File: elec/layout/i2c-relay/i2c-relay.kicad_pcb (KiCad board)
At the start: 2 copper layers, 7 parts, among them U2 10kΩ ±1% 62.5mW, U3 1kΩ ±1% 62.5mW

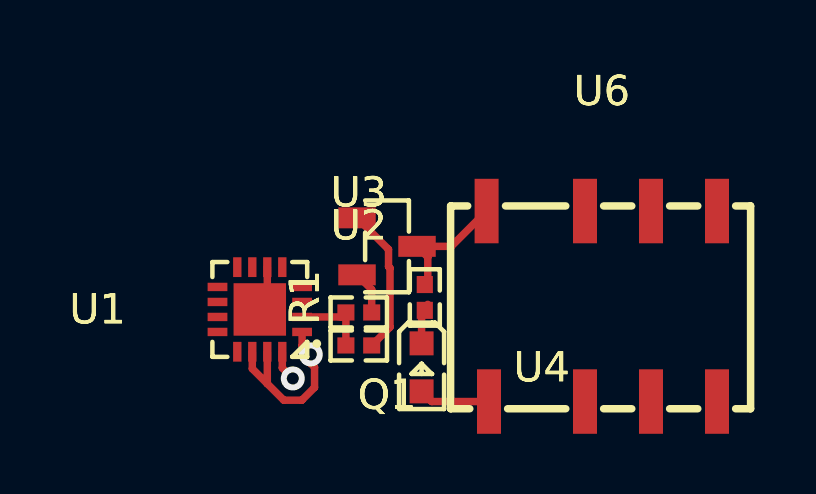
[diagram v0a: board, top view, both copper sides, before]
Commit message: update i2c relay
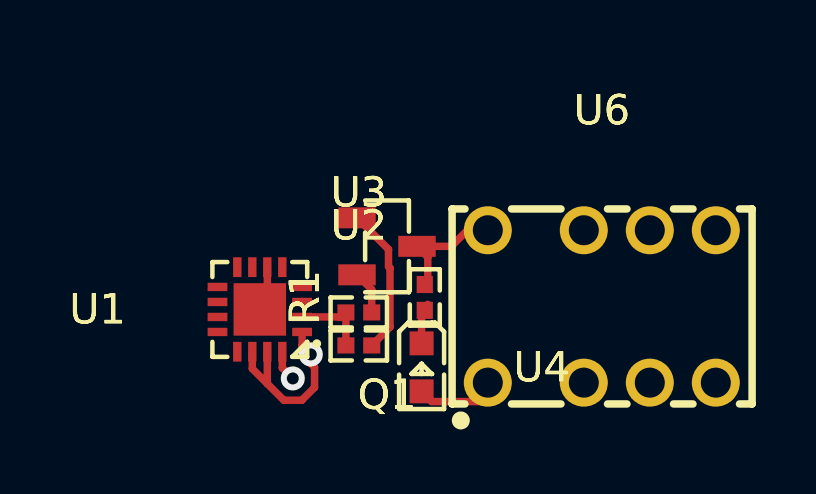
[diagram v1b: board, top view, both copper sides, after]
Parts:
- U6: footprint lib:RELAY-SMD_HFD4-5-SR -> atopile:RELAY-TH_HFDXXX-689a1e
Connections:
- net VCCP renamed RESET
- Q1 pad 2: gnd-1 -> gnd-3
- U1 pad 10: gpio_expander-net-3 -> gpio_expander-net-4
- U1 pad 12: line -> line-2
- U1 pad 13: line-2 -> line
- U1 pad 17: gnd -> gnd-1
- U1 pad 3: gpio_expander-net-5 -> gpio_expander-net
- U1 pad 4: gpio_expander-net-2 -> gpio_expander-net-1
- U1 pad 5: gpio_expander-net-1 -> gpio_expander-net-6
- U1 pad 6: gnd -> gnd-1
- U1 pad 7: gpio_expander-net -> gpio_expander-net-5
- U1 pad 8: gpio_expander-net-6 -> gpio_expander-net-3
- U1 pad 9: gpio_expander-net-4 -> gpio_expander-net-2
- U3 pad 2: gnd-1 -> gnd-3
- U6 pad 2: (no net) -> relay.relay.footprint.pins[1].net-net
- U6 pad 3: gnd-3 -> gnd-2
- U6 pad 4: gnd-2 -> gnd
- U6 pad 7: (no net) -> relay.relay.footprint.pins[6].net-net
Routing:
- net gnd: track 2.55 -> 0.00 mm, vias 1 -> 0
- net gnd-3: track 0.00 -> 1.46 mm
- net ADDR: track 0.00 -> 1.03 mm, vias 0 -> 1

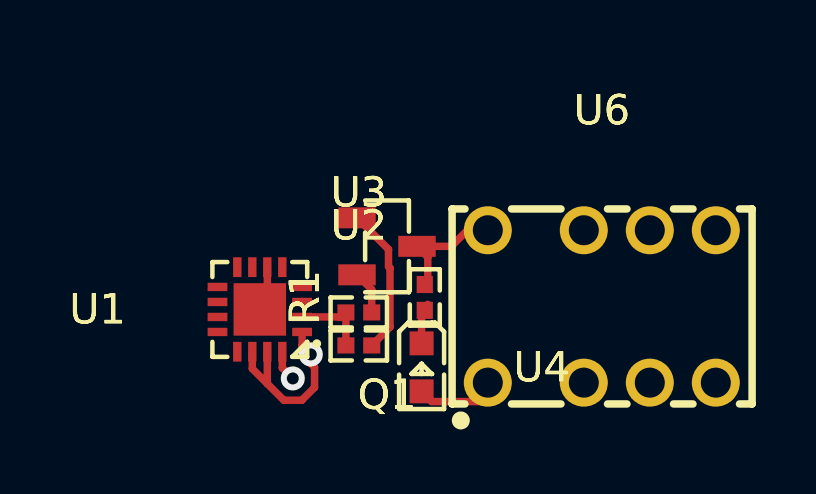
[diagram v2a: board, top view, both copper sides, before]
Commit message: fix i2c-relay layout
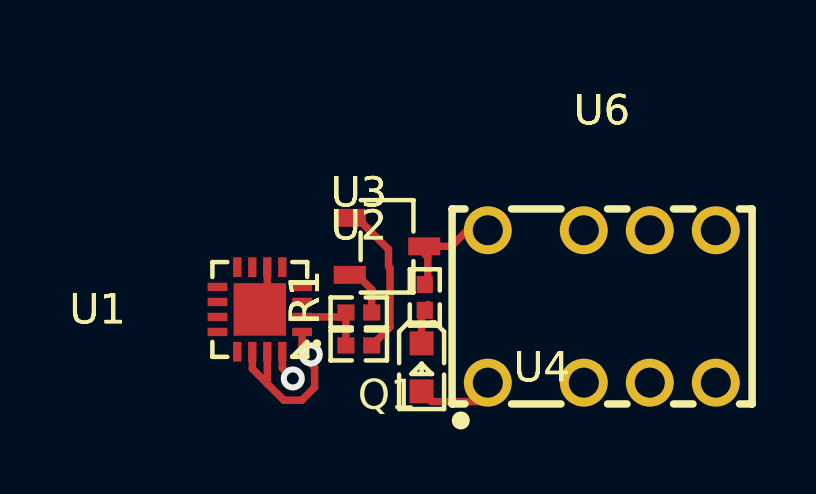
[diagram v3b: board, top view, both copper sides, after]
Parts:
- Q1: footprint atopile:SOT-23-3_L2.9-W1.3-P1.90-LS2.4-BR-688f29 -> atopile:SOT-23-3_L2.9-W1.6-P1.90-LS2.8-BR-186170
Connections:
- net RESET renamed VCCI
- net line-2 renamed SCL
- U1 pad 13: line -> SDA
- U1 pad 2: line-1 -> line
- U1 pad 3: gpio_expander-net -> gpio_expander-net-3
- U1 pad 4: gpio_expander-net-1 -> gpio_expander-net
- U1 pad 7: gpio_expander-net-5 -> gpio_expander-net-2
- U1 pad 8: gpio_expander-net-3 -> gpio_expander-net-1
- U1 pad 9: gpio_expander-net-2 -> gpio_expander-net-5
- U2 pad 1: line-1 -> line
- U3 pad 1: line-1 -> line
- U4 pad 2: hv-2 -> hv-1
- U6 pad 1: hv-2 -> hv-1
- U6 pad 5: hv -> hv-2
- U6 pad 6: hv-1 -> hv
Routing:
- net line-1: track 2.62 -> 0.00 mm
- net line: track 0.00 -> 2.62 mm
- net hv-2: track 2.39 -> 0.00 mm
- net hv-1: track 0.00 -> 2.39 mm

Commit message: building frozen
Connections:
- net VCCI renamed RESET
- Q1 pad 2: gnd-3 -> gnd
- U1 pad 10: gpio_expander-net-4 -> gpio_expander-net-5
- U1 pad 17: gnd-1 -> gnd-2
- U1 pad 3: gpio_expander-net-3 -> gpio_expander-net-1
- U1 pad 4: gpio_expander-net -> gpio_expander-net-6
- U1 pad 5: gpio_expander-net-6 -> gpio_expander-net
- U1 pad 6: gnd-1 -> gnd-2
- U1 pad 7: gpio_expander-net-2 -> gpio_expander-net-3
- U1 pad 8: gpio_expander-net-1 -> gpio_expander-net-4
- U1 pad 9: gpio_expander-net-5 -> gpio_expander-net-2
- U3 pad 2: gnd-3 -> gnd
- U4 pad 2: hv-1 -> hv
- U6 pad 1: hv-1 -> hv
- U6 pad 3: gnd-2 -> gnd-1
- U6 pad 4: gnd -> gnd-3
- U6 pad 5: hv-2 -> hv-1
- U6 pad 6: hv -> hv-2
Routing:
- net hv-1: track 2.39 -> 0.00 mm
- net hv: track 0.00 -> 2.39 mm
- net gnd-2: track 0.00 -> 1.51 mm
- net gnd-1: track 1.51 -> 0.00 mm
- net gnd-3: track 1.46 -> 0.00 mm
- net gnd: track 0.00 -> 1.46 mm
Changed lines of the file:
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@@
         (legacy_teardrops no)
     )
-    (paper A4)
+    (paper "A4")
     (layers
         (0 "F.Cu" signal)
@@
         (tenting front back)
         (pcbplotparams
-            (layerselection "0x00000000_00000000_55555555_5755f5ff")
-            (plot_on_all_layers_selection "0x00000000_00000000_00000000_00000000")
+            (layerselection 0x00000000_00000000_55555555_5755f5ff)
+            (plot_on_all_layers_selection 0x00000000_00000000_00000000_00000000)
             (disableapertmacros no)
             (usegerberextensions no)
@@
             (dxfusepcbnewfont yes)
             (psnegative no)
+            (psa4output no)
             (plot_black_and_white yes)
-            (psa4output no)
+            (plotinvisibletext no)
+            (sketchpadsonfab no)
             (plotreference yes)
+            (plotvalue yes)
             (plotpadnumbers no)
             (hidednponfab no)
             (sketchdnponfab yes)
             (crossoutdnponfab yes)
-            (plotvalue yes)
             (plotfptext yes)
-            (plotinvisibletext no)
-            (sketchpadsonfab no)
             (subtractmaskfromsilk no)
             (outputformat 1)
@@
     )
     (net 0 "")
-    (net 1 "gpio_expander-net")
+    (net 1 "gpio_expander-net-6")
     (net 2 "SCL")
-    (net 3 "gpio_expander-net-4")
-    (net 4 "hv")
-    (net 5 "gpio_expander-net-2")
-    (net 6 "gpio_expander-net-5")
-    (net 7 "hv-1")
+    (net 3 "gpio_expander-net-5")
+    (net 4 "hv-2")
+    (net 5 "gpio_expander-net-3")
+    (net 6 "gpio_expander-net-2")
+    (net 7 "hv")
     (net 8 "line")
-    (net 9 "gnd-2")
+    (net 9 "gnd-1")
     (net 10 "INT")
-    (net 11 "gpio_expander-net-1")
-    (net 12 "VCCI")
-    (net 13 "hv-2")
+    (net 11 "gpio_expander-net-4")
+    (net 12 "RESET")
+    (net 13 "hv-1")
     (net 14 "SDA")
-    (net 15 "gpio_expander-net-6")
-    (net 16 "gnd")
-    (net 17 "gnd-3")
+    (net 15 "gpio_expander-net")
+    (net 16 "gnd-3")
+    (net 17 "gnd")
     (net 18 "gate")
-    (net 19 "gpio_expander-net-3")
-    (net 20 "gnd-1")
+    (net 19 "gpio_expander-net-1")
+    (net 20 "gnd-2")
     (net 21 "relay-gnd")
     (net 22 "cathode")
@@
             (size 0.57 0.54)
             (layers "F.Cu" "F.Mask" "F.Paste")
-            (net 17 "gnd-3")
+            (net 17 "gnd")
             (remove_unused_layers yes)
             (keep_end_layers yes)
@@
             (size 0.8 0.8)
             (layers "F.Cu" "F.Mask" "F.Paste")
-            (net 7 "hv-1")
+            (net 7 "hv")
             (remove_unused_layers yes)
             (keep_end_layers yes)
@@
             (drill 0.999998)
             (layers "*.Cu" "*.Mask")
-            (net 7 "hv-1")
+            (net 7 "hv")
             (remove_unused_layers no)
             (keep_end_layers yes)
@@
             (drill 0.999998)
             (layers "*.Cu" "*.Mask")
-            (net 9 "gnd-2")
+            (net 9 "gnd-1")
             (remove_unused_layers no)
             (keep_end_layers yes)
@@
             (drill 0.999998)
             (layers "*.Cu" "*.Mask")
-            (net 16 "gnd")
+            (net 16 "gnd-3")
             (remove_unused_layers no)
             (keep_end_layers yes)
@@
             (drill 0.999998)
             (layers "*.Cu" "*.Mask")
-            (net 13 "hv-2")
+            (net 13 "hv-1")
             (remove_unused_layers no)
             (keep_end_layers yes)
@@
             (drill 0.999998)
             (layers "*.Cu" "*.Mask")
-            (net 4 "hv")
+            (net 4 "hv-2")
             (remove_unused_layers no)
             (keep_end_layers yes)
@@
             (size 1.07 0.6)
             (layers "F.Cu" "F.Paste" "F.Mask")
-            (net 17 "gnd-3")
+            (net 17 "gnd")
             (remove_unused_layers yes)
             (keep_end_layers yes)
@@
             (size 0.28 0.66)
             (layers "F.Cu" "F.Mask" "F.Paste")
-            (net 12 "VCCI")
+            (net 12 "RESET")
             (remove_unused_layers yes)
             (keep_end_layers yes)
@@
             (size 0.28 0.66)
             (layers "F.Cu" "F.Mask" "F.Paste")
-            (net 19 "gpio_expander-net-3")
+            (net 19 "gpio_expander-net-1")
             (remove_unused_layers yes)
             (keep_end_layers yes)
@@
             (size 0.28 0.66)
             (layers "F.Cu" "F.Mask" "F.Paste")
-            (net 1 "gpio_expander-net")
+            (net 1 "gpio_expander-net-6")
             (remove_unused_layers yes)
             (keep_end_layers yes)
@@
             (size 0.66 0.28)
             (layers "F.Cu" "F.Mask" "F.Paste")
-            (net 15 "gpio_expander-net-6")
+            (net 15 "gpio_expander-net")
             (remove_unused_layers yes)
             (keep_end_layers yes)
@@
             (size 0.66 0.28)
             (layers "F.Cu" "F.Mask" "F.Paste")
-            (net 20 "gnd-1")
+            (net 20 "gnd-2")
             (remove_unused_layers yes)
             (keep_end_layers yes)
@@
             (size 0.66 0.28)
             (layers "F.Cu" "F.Mask" "F.Paste")
-            (net 5 "gpio_expander-net-2")
+            (net 5 "gpio_expander-net-3")
             (remove_unused_layers yes)
             (keep_end_layers yes)
@@
             (size 0.66 0.28)
             (layers "F.Cu" "F.Mask" "F.Paste")
-            (net 11 "gpio_expander-net-1")
+            (net 11 "gpio_expander-net-4")
             (remove_unused_layers yes)
             (keep_end_layers yes)
@@
             (size 0.28 0.66)
             (layers "F.Cu" "F.Mask" "F.Paste")
-            (net 6 "gpio_expander-net-5")
+            (net 6 "gpio_expander-net-2")
             (remove_unused_layers yes)
             (keep_end_layers yes)
@@
             (size 0.28 0.66)
             (layers "F.Cu" "F.Mask" "F.Paste")
-            (net 3 "gpio_expander-net-4")
+            (net 3 "gpio_expander-net-5")
             (remove_unused_layers yes)
             (keep_end_layers yes)
@@
             (size 0.66 0.28)
             (layers "F.Cu" "F.Mask" "F.Paste")
-            (net 12 "VCCI")
+            (net 12 "RESET")
             (remove_unused_layers yes)
             (keep_end_layers yes)
@@
             (size 0.66 0.28)
             (layers "F.Cu" "F.Mask" "F.Paste")
-            (net 12 "VCCI")
+            (net 12 "RESET")
             (remove_unused_layers yes)
             (keep_end_layers yes)
@@
             (size 1.75 1.75)
             (layers "F.Cu" "F.Mask" "F.Paste")
-            (net 20 "gnd-1")
-            (remove_unused_layers yes)
-            (keep_end_layers yes)
+            (net 20 "gnd-2")
+            (remove_unused_layers yes)
+            (keep_end_layers yes)
